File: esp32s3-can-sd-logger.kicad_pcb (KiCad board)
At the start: 4 copper layers, 84 x 80 mm, 183 parts, among them J1 PWR + CAN harness, J10 Sensor harness, J2 USB-C, J3 UART0, J4 I2C / Qwiic, J5 SPI, J6 WS2812, J7 Spare IO, J8 Rail break-out, J9 microSD push-pull, Q1 100V 6.8mOhm N-ch, Q2 -20V 2.3A P-ch, Q3 60V 300mA N-ch, SW1 RESET, SW2 BOOT, U1 LM74700-Q1, U2 LM5164 (5V), U3 LM5164 (3V3), U4 ESP32-S3-WROOM-1-N16R8, U5 USBLC6-2SC6, U6 74AHCT1G125, U7 TJA1051T/3, U8 ADS1115

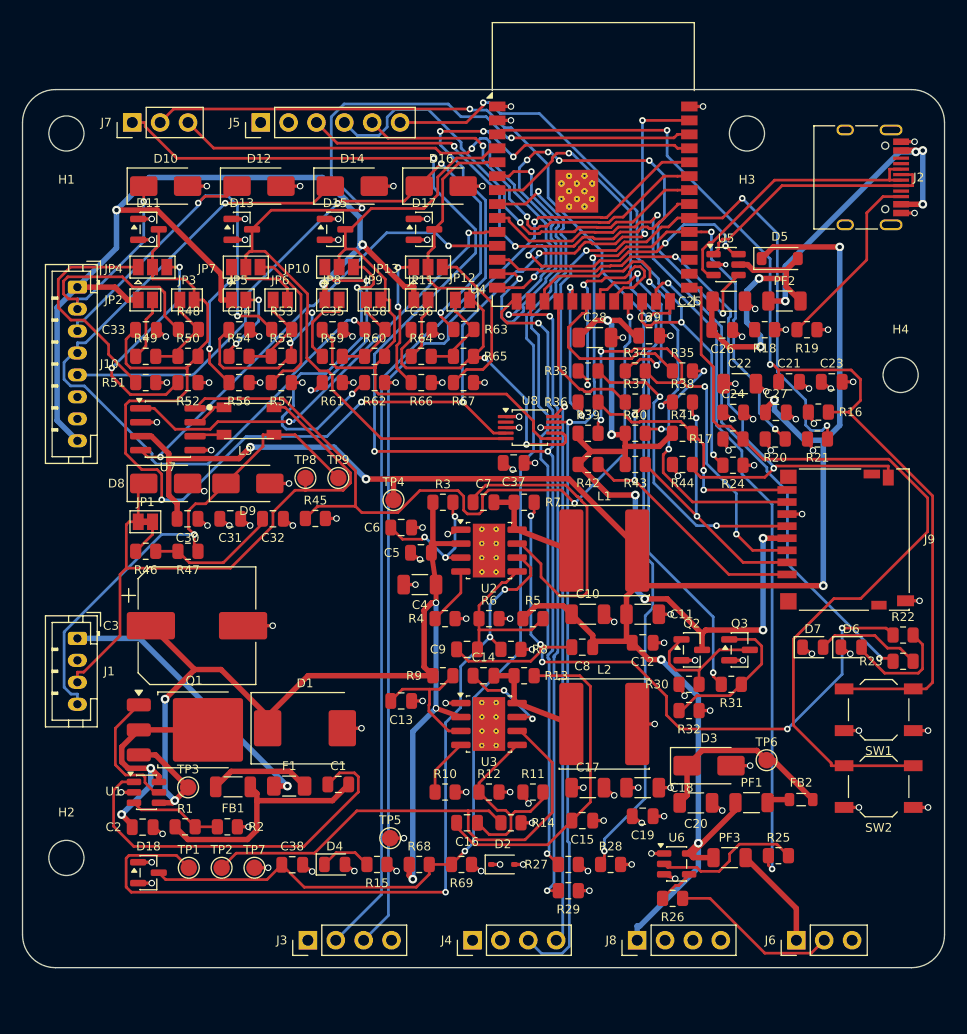
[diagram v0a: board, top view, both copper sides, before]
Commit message: Rev B is fully routed: zero DRC errors, nothing unconnected
84 x 84 mm, 1447 tracks, 258 vias, 179 footprints, 106 nets.

The last few connections were never routing problems. Each one was a part
sited away from the net it belongs to, and the autorouter reporting "no
path at any width" was telling the truth:

  +5VS  the sensor rail's source (PF1/FB2/D3) sat on the right beside the
        WS2812 header while everything it feeds -- the sensor harness and
        all four channel pull-ups -- is on the left. The net existed as
        two complete halves with a 45 mm gap through buck islands and the
        SD socket. Moved the source to the harness side.
  IO46  the strapping pull-downs were parked in the bottom band while
        IO3/IO45/IO46 run from the module's south pads to J7 at the top
        left, so R29 needed a trace the length of the board to reach its
        own net. Moved them under the module's south pads.

Adding router passes had never touched either. Moving the parts fixed
both immediately -- worth remembering next time a net "cannot be routed".

Also in this pass:

  - One LED. D6 (amber) and D7 (blue) and their resistors are gone; D4
    green stays on +3V3, which is the right rail to watch because it only
    lights if the whole chain came through -- battery, ideal diode, both
    converters. That also retires review item 11.2.10, the blue emitter
    that would have been near-invisible on a 3.288 V rail.
  - J7 grows to six pins: the three strapping pins, the two GPIOs freed
    by the LEDs (IO15/IO16), and a ground pin. The missing ground was
    review item 13.4.13.
  - USB_CC1 gets a Fine netclass at 0.2 mm. There is no route at 0.25 mm
    -- the USB-C pads are on 0.5 mm pitch and will not pass it -- and CC
    carries under a milliamp through a 5.1k pull-down.
  - build_board.py takes a lock. Two builds sharing the board file is how
    one run died at "Specctra session import failed" after ten minutes,
    when a second build regenerated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
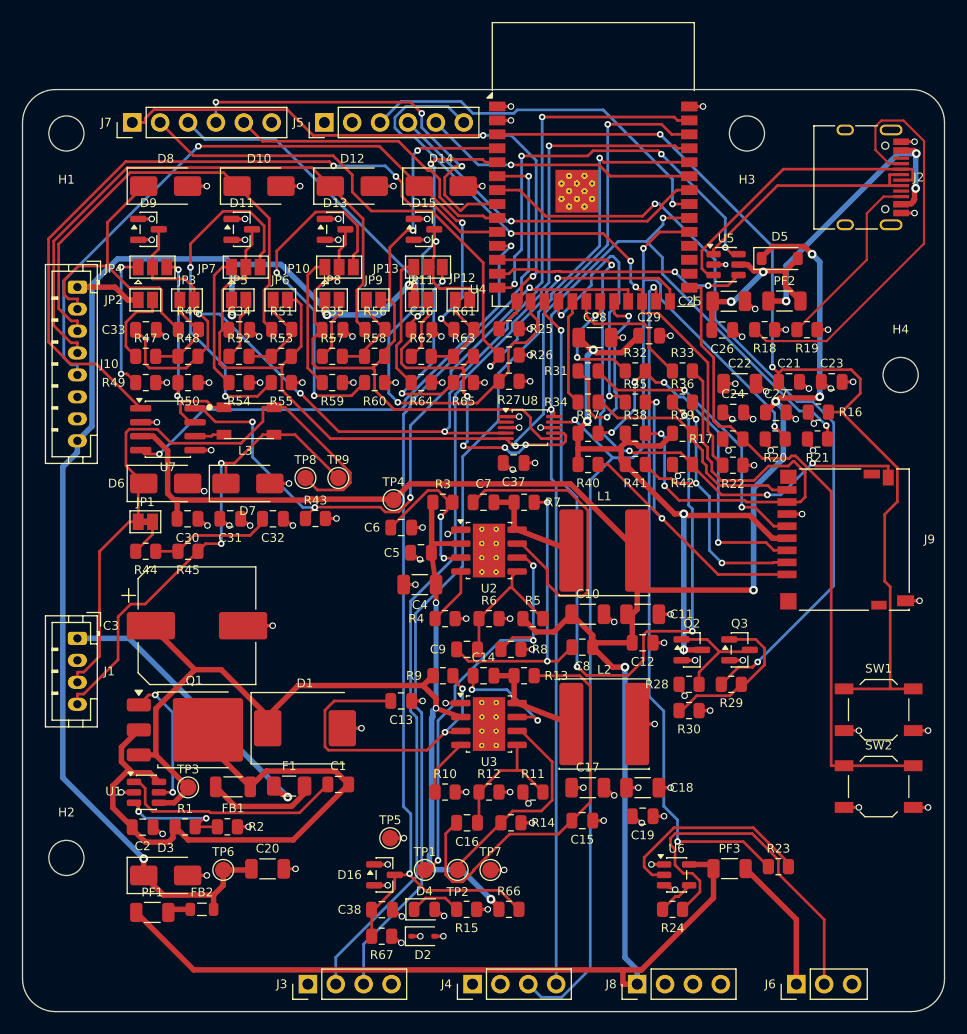
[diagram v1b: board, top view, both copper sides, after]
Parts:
- removed D17, D18: BAT54S, SOT-23
- removed R68: 100k, R_0805_2012Metric
- removed R69: 8.2k, R_0805_2012Metric
- D16: value SMAJ40CA -> BAT54S; footprint D_SMA -> SOT-23
- D6: value amber -> SMAJ26CA; footprint LED_0805_2012Metric -> D_SMA
- D7: value blue -> SMAJ26CA; footprint LED_0805_2012Metric -> D_SMA
- D8: value SMAJ26CA -> SMAJ40CA
- D9: value SMAJ26CA -> BAT54S; footprint D_SMA -> SOT-23
- J7: footprint PinHeader_1x03_P2.54mm_Vertical -> PinHeader_1x06_P2.54mm_Vertical
- R22, R48, R53, R58, R63: value 1k -> 10k
- R23: value 150 -> 33
- R24: value 10k -> 100
- R25, R37, R38: value 33 -> 10k
- R26: value 100 -> 10k
- R28: value 10k -> 100k
- R29: value 10k -> 1k
- R31: value 1k -> 33
- R32: value 100k -> 33
- R42: value 10k -> 47k
- R44: value 47k -> 60.4
- R45: value 10k -> 60.4
- R46: value 60.4 -> 1k
- R47: value 60.4 -> 2.49k
- R49, R54, R59, R64: value 2.49k -> 15k
- R50, R55, R60, R65: value 10k -> 2.21k
- R51, R56, R61: value 15k -> 1k
- R52, R57, R62: value 2.21k -> 2.49k
- R66: value 15k -> 100k
- R67: value 2.21k -> 8.2k
- moved D6 64.2 mm to (13.0, 35.9)
- moved D16 63.0 mm to (33.0, 71.5)
- moved FB2 55.5 mm to (16.3, 74.7)
- moved PF1 55.5 mm to (11.8, 75.0)
- moved R25 53.9 mm to (44.3, 21.8)
- moved D7 53.6 mm to (20.5, 35.9)
- moved R26 51.7 mm to (44.3, 24.2)
- moved R67 51.0 mm to (32.7, 77.1)
- moved D3 50.5 mm to (13.0, 71.6)
- moved TP6 50.5 mm to (18.3, 71.1)
- moved R44 49.5 mm to (11.2, 42.1)
- moved R66 48.7 mm to (44.3, 74.7)
- moved R27 44.3 mm to (44.3, 26.6)
- moved R24 40.8 mm to (59.2, 74.7)
- moved C20 39.5 mm to (22.3, 71.0)
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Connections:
- D10 pad 1: AIN1_IN -> AIN2_IN
- D11 pad 3: AIN1 -> AIN2
- D12 pad 1: AIN2_IN -> AIN3_IN
- D13 pad 3: AIN2 -> AIN3
- D14 pad 1: AIN3_IN -> AIN4_IN
- D15 pad 3: AIN3 -> AIN4
- D16 pad 1: AIN4_IN -> GND
- D16 pad 2: GND -> +3V3
- D6 pad 1: GND -> CAN_H
- D6 pad 2: LED1_A -> GND
- D7 pad 1: GND -> CAN_L
- D7 pad 2: LED2_A -> GND
- D8 pad 1: CAN_H -> AIN1_IN
- D9 pad 1: CAN_L -> GND
- D9 pad 2: GND -> +3V3
- R22 pad 1: LED1 -> SPI_CS
- R22 pad 2: LED1_A -> +3V3
- R23 pad 1: LED2 -> LED_DIN_MCU
- R23 pad 2: LED2_A -> LED_DIN_A
- R24 pad 1: SPI_CS -> LED_DIN
- R24 pad 2: +3V3 -> LED_DIN_J
- R25 pad 1: LED_DIN_MCU -> IO3
- R25 pad 2: LED_DIN_A -> GND
- R26 pad 1: LED_DIN -> IO45
- R26 pad 2: LED_DIN_J -> GND
- R27 pad 1: IO3 -> IO46
- R28 pad 1: IO45 -> +3V3
- R28 pad 2: GND -> SD_PG
- R29 pad 1: IO46 -> SD_PWR_EN
- R29 pad 2: GND -> SD_EN_G
- R30 pad 1: +3V3 -> SD_EN_G
- R30 pad 2: SD_PG -> GND
- R31 pad 1: SD_PWR_EN -> SD_CLK
- R31 pad 2: SD_EN_G -> SD_CLK_C
- R32 pad 1: SD_EN_G -> SD_CMD
- R32 pad 2: GND -> SD_CMD_C
- R33 pad 1: SD_CLK -> SD_D0
- R33 pad 2: SD_CLK_C -> SD_D0_C
- R34 pad 1: SD_CMD -> SD_D1
- R34 pad 2: SD_CMD_C -> SD_D1_C
- R35 pad 1: SD_D0 -> SD_D2
- R35 pad 2: SD_D0_C -> SD_D2_C
- R36 pad 1: SD_D1 -> SD_D3
- R36 pad 2: SD_D1_C -> SD_D3_C
- R37 pad 1: SD_D2 -> SD_VDD
- R37 pad 2: SD_D2_C -> SD_CMD_C
- R38 pad 1: SD_D3 -> SD_VDD
- R38 pad 2: SD_D3_C -> SD_D0_C
- R39 pad 2: SD_CMD_C -> SD_D1_C
- R40 pad 2: SD_D0_C -> SD_D2_C
- R41 pad 2: SD_D1_C -> SD_D3_C
- R42 pad 1: SD_VDD -> +3V3
- R42 pad 2: SD_D2_C -> SD_CD
- R43 pad 1: SD_VDD -> CAN_S
- R43 pad 2: SD_D3_C -> GND
- R44 pad 1: +3V3 -> TERM_A
- R44 pad 2: SD_CD -> CAN_SPLIT
- R45 pad 1: CAN_S -> CAN_SPLIT
- R45 pad 2: GND -> CAN_L
- R46 pad 1: TERM_A -> AIN1_IN
- R46 pad 2: CAN_SPLIT -> AIN1_A
- R47 pad 1: CAN_SPLIT -> AIN1_PU
- R47 pad 2: CAN_L -> AIN1_A
- R48 pad 1: AIN1_IN -> AIN1_A
- R48 pad 2: AIN1_A -> AIN1
- R49 pad 1: AIN1_PU -> AIN1_R1
- R49 pad 2: AIN1_A -> GND
- R50 pad 1: AIN1_A -> AIN1_R2
- R50 pad 2: AIN1 -> GND
- R51 pad 1: AIN1_R1 -> AIN2_IN
- R51 pad 2: GND -> AIN2_A
- R52 pad 1: AIN1_R2 -> AIN2_PU
- R52 pad 2: GND -> AIN2_A
- R53 pad 1: AIN2_IN -> AIN2_A
- R53 pad 2: AIN2_A -> AIN2
- R54 pad 1: AIN2_PU -> AIN2_R1
- R54 pad 2: AIN2_A -> GND
- R55 pad 1: AIN2_A -> AIN2_R2
- R55 pad 2: AIN2 -> GND
- R56 pad 1: AIN2_R1 -> AIN3_IN
- R56 pad 2: GND -> AIN3_A
- R57 pad 1: AIN2_R2 -> AIN3_PU
- R57 pad 2: GND -> AIN3_A
- R58 pad 1: AIN3_IN -> AIN3_A
- R58 pad 2: AIN3_A -> AIN3
- R59 pad 1: AIN3_PU -> AIN3_R1
- R59 pad 2: AIN3_A -> GND
- R60 pad 1: AIN3_A -> AIN3_R2
- R60 pad 2: AIN3 -> GND
- R61 pad 1: AIN3_R1 -> AIN4_IN
- R61 pad 2: GND -> AIN4_A
- R62 pad 1: AIN3_R2 -> AIN4_PU
- R62 pad 2: GND -> AIN4_A
- R63 pad 1: AIN4_IN -> AIN4_A
- R63 pad 2: AIN4_A -> AIN4
- R64 pad 1: AIN4_PU -> AIN4_R1
- R64 pad 2: AIN4_A -> GND
- R65 pad 1: AIN4_A -> AIN4_R2
- R65 pad 2: AIN4 -> GND
- R66 pad 1: AIN4_R1 -> +VBAT
- R66 pad 2: GND -> VBAT_SNS
- R67 pad 1: AIN4_R2 -> VBAT_SNS
- U4 pad 8: LED1 -> IO15
- U4 pad 9: LED2 -> IO16
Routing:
- net LED1: track 93.1 -> 0.00 mm, vias 4 -> 0
- net IO3: track 133.7 -> 56.9 mm, vias 5 -> 2
- net LED2: track 67.1 -> 0.00 mm, vias 2 -> 0
- net IO46: track 108.5 -> 59.0 mm, vias 4 -> 1
- net IO45: track 111.2 -> 68.3 mm, vias 3 -> 2
- net SD_D3: track 27.4 -> 70.0 mm, vias 2 -> 4
- net +5V: track 186.9 -> 227.5 mm, vias 7 -> 5
- net USB_CC1: track 0.00 -> 39.3 mm
- net IO15: track 0.00 -> 36.6 mm, vias 0 -> 3
- net USB_DM: track 59.0 -> 23.2 mm, vias 6 -> 2
- net PG_5V: track 74.8 -> 39.0 mm
- net PG_3V3: track 47.8 -> 19.3 mm
- net IO16: track 0.00 -> 27.6 mm
- net CAN_TX: track 41.4 -> 67.5 mm
- net AIN1: track 124.4 -> 103.4 mm, vias 6 -> 4
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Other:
- board size 84 x 80 mm -> 84 x 84 mm

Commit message: Turn the USB-C round, clamp ahead of the FET, draw the last two blocks
Two review findings from Matt, both correct:

  - The USB-C receptacle faced the wrong way. Its fab outline runs
    y -3.65..+3.65 and the signal pads sit at y -4.04, outside it: the
    contacts leave the REAR of the shell, so at 0 degrees the mouth faces
    +y, and at the 270 it was placed at the opening pointed back into the
    middle of the board. At 90 the mouth ends ~2 mm inside the right edge
    -- the plug approaches over the top of the laminate, so those last
    2 mm are not in its way -- and the pad row faces inboard, which is
    where the D+/D- via columns and the USBLC6 already were.

  - The transient clamp was behind the reverse-battery FET, which leaves
    Q1 and the LM74700 exposed to whatever arrives on the harness: on a
    negative transient Q1 turns off and stands the whole pulse across its
    drain-source, and ISO 7637-2 pulse 1 (-100V) and 3a (-150V) both
    exceed its 100V rating. It now sits on VBAT_F, straight after the
    fuse and ahead of the ferrite and the FET.

    It also changes from SMCJ40A to SMCJ40CA. A unidirectional part in
    that position forward-conducts on a sustained reverse connection and
    blows the fuse -- exactly the outcome the ideal diode exists to
    avoid. Bidirectional stands off 40V either way, so -14V reverse
    battery is still Q1's job to block and only real transients clamp.
    Needs an LCSC pick at order time, as the SMCJ40A did.

The power front end and the USB port are now hand-drawn blocks too, so
every recurring circuit on the board comes from gen/sch_blocks.py.

Board rerouted from scratch at 60 autoroute passes: 0 DRC violations,
0 unconnected. Netlist matches node for node, ERC clean. fab/ regenerated.

Co-Authored-By: Claude Opus 5 <noreply@anthropic.com>
Claude-Session: https://claude.ai/code/session_01DhNbL25h25p8VFCjRfJik9
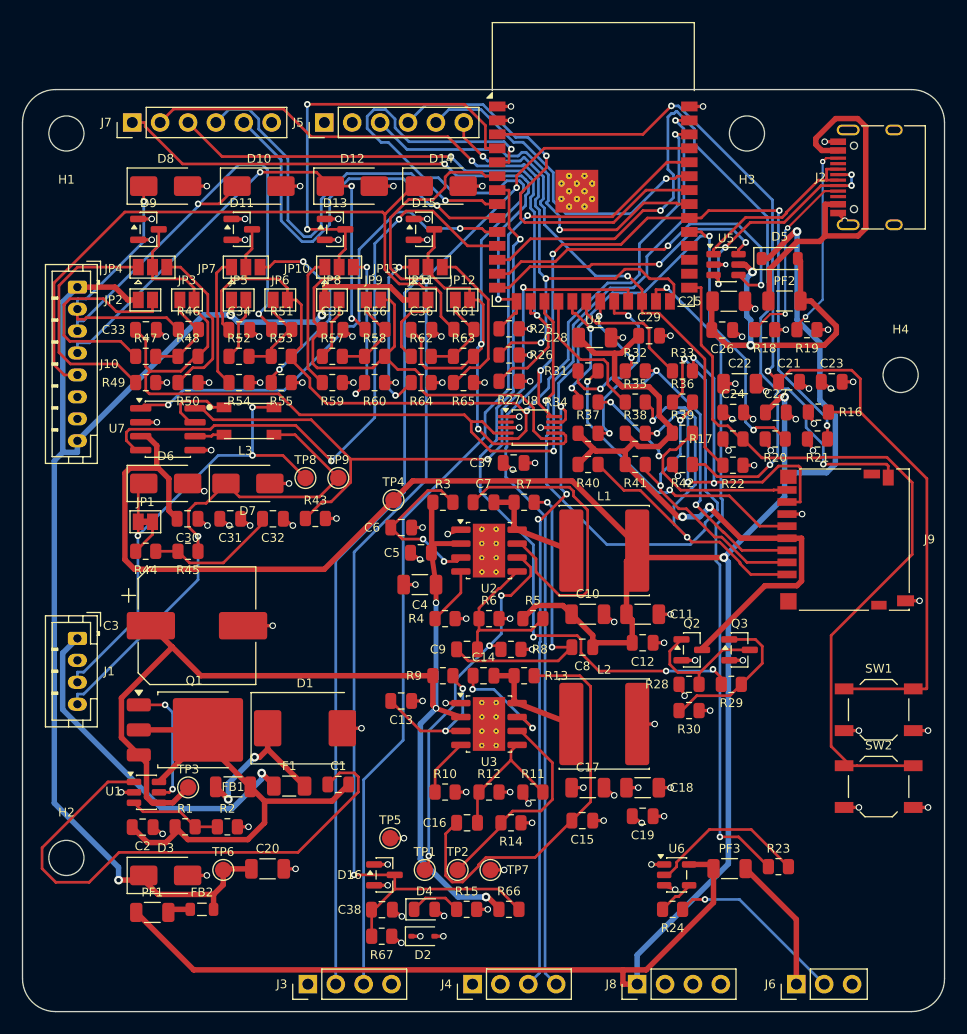
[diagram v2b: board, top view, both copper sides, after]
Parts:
- D1: value SMCJ40A -> SMCJ40CA
- moved J2 2.35 mm to (78.3, 8.00), turned to 90 degrees
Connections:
- D1 pad 1: +VBAT -> VBAT_F
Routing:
- net +5V: track 227.5 -> 262.5 mm, vias 5 -> 3
- net AIN4: track 62.6 -> 95.3 mm, vias 7 -> 3
- net SD_CD: track 57.4 -> 88.2 mm, vias 4 -> 3
- net VCAP: track 20.7 -> 50.2 mm
- net CAN_TX: track 67.5 -> 44.4 mm
- net USB_CC1: track 39.3 -> 17.3 mm, vias 0 -> 2
- net AIN3_R2: track 33.0 -> 14.5 mm
- net LED_DIN_J: track 32.8 -> 16.5 mm, vias 0 -> 1
- net I2C_SCL: track 104.4 -> 120.2 mm, vias 3 -> 4
- net EN_3V3: track 29.1 -> 13.6 mm
- net VBUS: track 17.9 -> 32.5 mm
- net AIN2_R2: track 32.3 -> 18.4 mm
- net SD_D3: track 70.0 -> 56.4 mm, vias 4 -> 2
- net AIN3: track 71.4 -> 84.1 mm
- net AIN1_PU: track 7.37 -> 20.0 mm
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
